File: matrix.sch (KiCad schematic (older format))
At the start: 84 parts

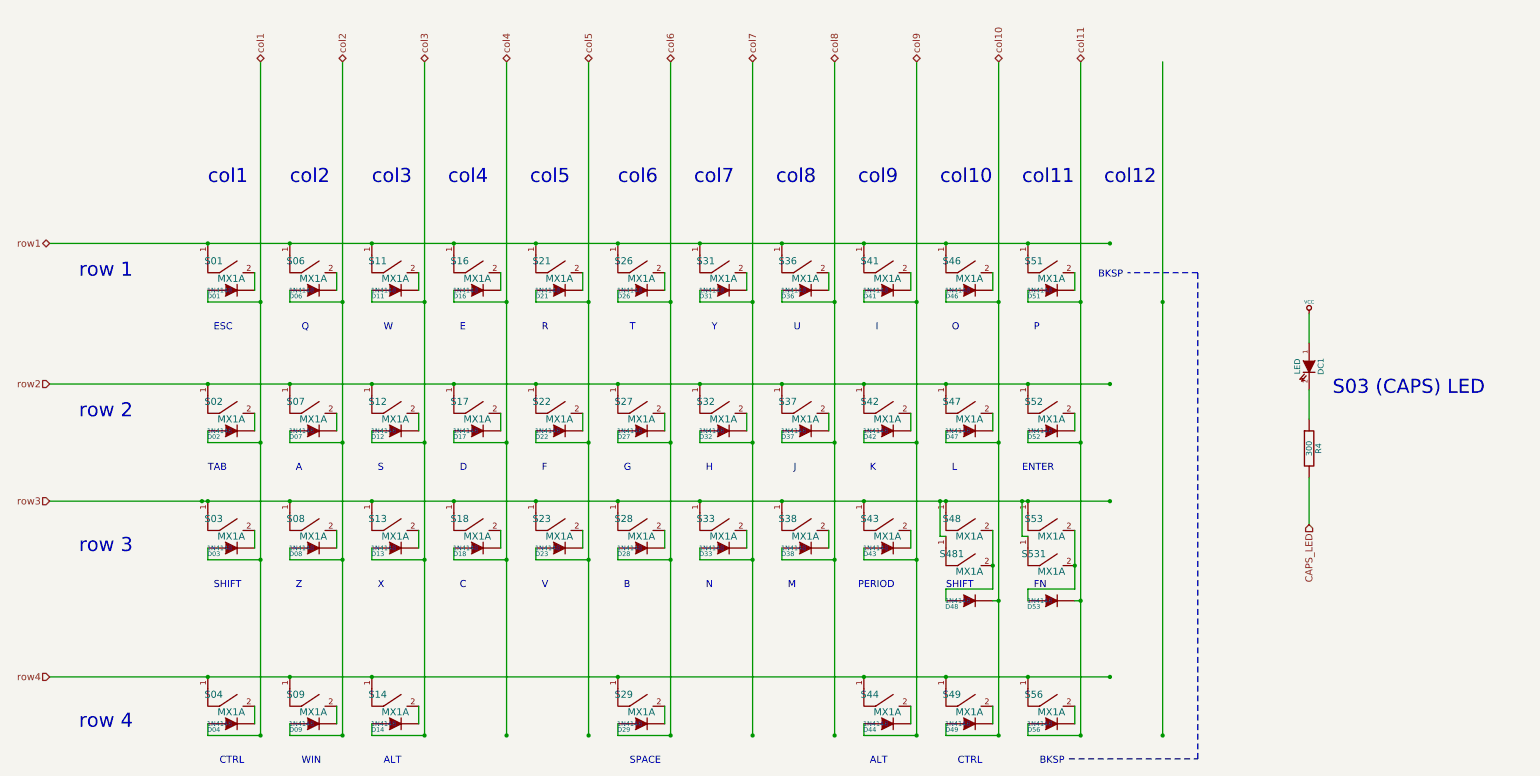
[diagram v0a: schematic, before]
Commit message: Change the cyrstal footprint / correct two wrong diode directions
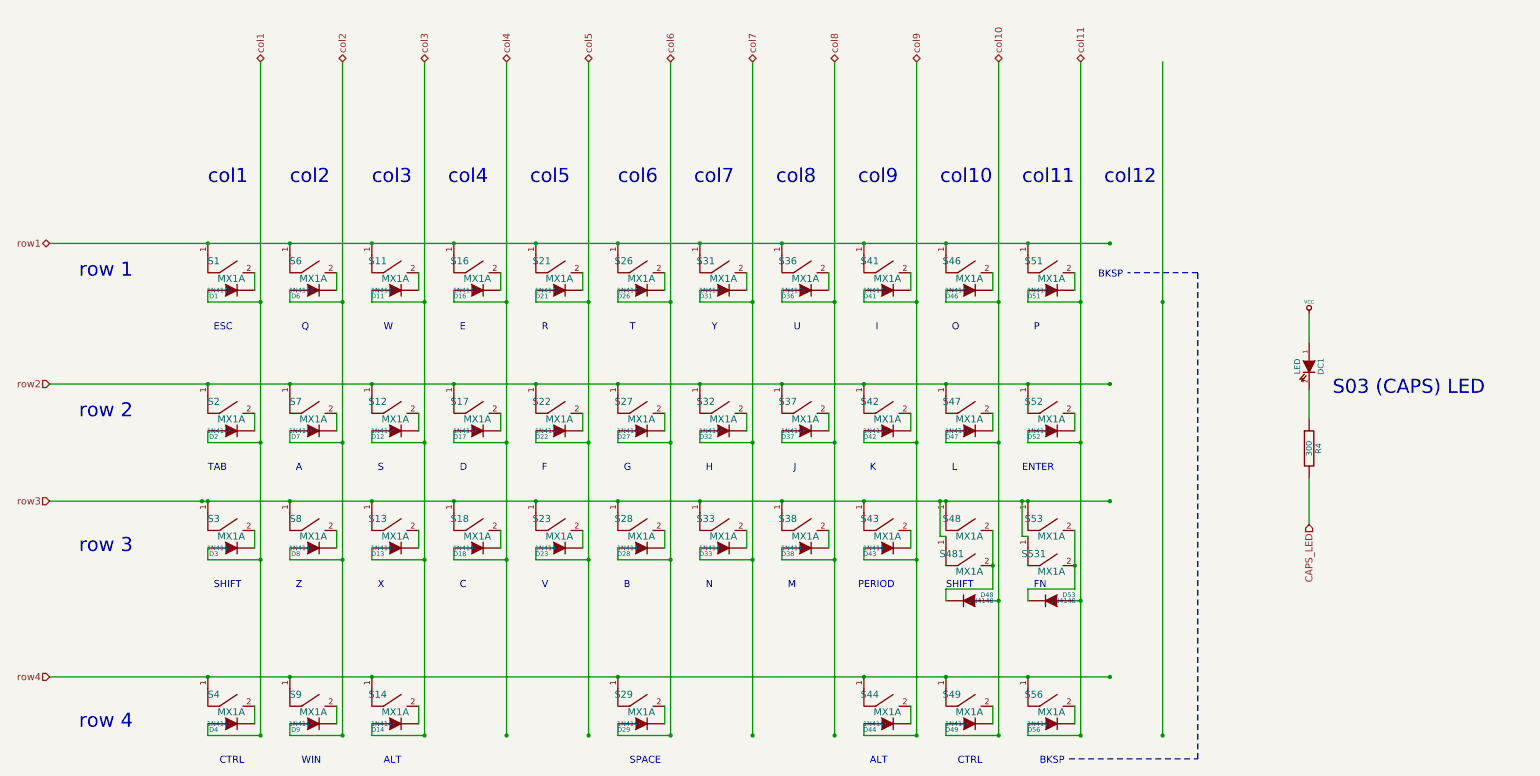
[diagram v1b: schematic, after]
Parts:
- renumbered D01 to D1, D02 to D2, D03 to D3, D04 to D4, D06 to D6, D07 to D7, D08 to D8, D09 to D9, S01 to S1, S02 to S2, S03 to S3, S04 to S4, S06 to S6, S07 to S7, S08 to S8, S09 to S9
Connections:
- net col10: now also D48.1 (A); no longer D48.2 (K)
- net col11: now also D53.1 (A); no longer D53.2 (K)
- net at S48.2, S481.2: now also D48.2 (K); no longer D48.1 (A)
- net at S53.2, S531.2: now also D53.2 (K); no longer D53.1 (A)
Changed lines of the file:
@@
-EESchema Schematic File Version 2  date 11/23/2013 1:19:47 PM
+EESchema Schematic File Version 2
 LIBS:power
 LIBS:mx1a-simple
@@
 LIBS:usb_ports
 LIBS:keyboard-cache
-EELAYER 27 0
+EELAYER 25 0
 EELAYER END
 $Descr A3 16535 11693
@@
 $EndDescr
 $Comp
-L MX1A S01
+L MX1A S1
 U 1 1 5040DD75
 P 3350 3350
-F 0 "S01" H 3200 3600 60  0000 C CNN
+F 0 "S1" H 3200 3600 60  0000 C CNN
 F 1 "MX1A" H 3350 3450 60  0000 C CNN
 F 2 "" H 3350 3350 60  0001 C CNN
@@
 $EndComp
 $Comp
-L MX1A S06
+L MX1A S6
 U 1 1 5040DD84
 P 4050 3350
-F 0 "S06" H 3900 3600 60  0000 C CNN
+F 0 "S6" H 3900 3600 60  0000 C CNN
 F 1 "MX1A" H 4050 3450 60  0000 C CNN
 F 2 "" H 4050 3350 60  0001 C CNN
@@
 $EndComp
 $Comp
-L MX1A S02
+L MX1A S2
 U 1 1 5040DDF7
 P 3350 4550
-F 0 "S02" H 3200 4800 60  0000 C CNN
+F 0 "S2" H 3200 4800 60  0000 C CNN
 F 1 "MX1A" H 3350 4650 60  0000 C CNN
 F 2 "" H 3350 4550 60  0001 C CNN
@@
 $EndComp
 $Comp
-L MX1A S07
+L MX1A S7
 U 1 1 5040DDFD
 P 4050 4550
-F 0 "S07" H 3900 4800 60  0000 C CNN
+F 0 "S7" H 3900 4800 60  0000 C CNN
 F 1 "MX1A" H 4050 4650 60  0000 C CNN
 F 2 "" H 4050 4550 60  0001 C CNN
@@
 $EndComp
 $Comp
-L MX1A S03
+L MX1A S3
 U 1 1 5040DE57
 P 3350 5550
-F 0 "S03" H 3200 5800 60  0000 C CNN
+F 0 "S3" H 3200 5800 60  0000 C CNN
 F 1 "MX1A" H 3350 5650 60  0000 C CNN
 F 2 "" H 3350 5550 60  0001 C CNN
@@
 $EndComp
 $Comp
-L MX1A S08
+L MX1A S8
 U 1 1 5040DE5D
 P 4050 5550
-F 0 "S08" H 3900 5800 60  0000 C CNN
+F 0 "S8" H 3900 5800 60  0000 C CNN
 F 1 "MX1A" H 4050 5650 60  0000 C CNN
 F 2 "" H 4050 5550 60  0001 C CNN
@@
 $EndComp
 $Comp
-L MX1A S09
+L MX1A S9
 U 1 1 5040DEBD
 P 4050 7050
-F 0 "S09" H 3900 7300 60  0000 C CNN
+F 0 "S9" H 3900 7300 60  0000 C CNN
 F 1 "MX1A" H 4050 7150 60  0000 C CNN
 F 2 "" H 4050 7050 60  0001 C CNN
@@
 $EndComp
 $Comp
-L MX1A S04
+L MX1A S4
 U 1 1 5040DEB7
 P 3350 7050
-F 0 "S04" H 3200 7300 60  0000 C CNN
+F 0 "S4" H 3200 7300 60  0000 C CNN
 F 1 "MX1A" H 3350 7150 60  0000 C CNN
 F 2 "" H 3350 7050 60  0001 C CNN
@@
 col11
 $Comp
-L VCC #PWR032
+L VCC #PWR028
 U 1 1 5043970C
 P 12550 3550
-F 0 "#PWR032" H 12550 3650 30  0001 C CNN
+F 0 "#PWR028" H 12550 3650 30  0001 C CNN
 F 1 "VCC" H 12550 3650 30  0000 C CNN
 F 2 "" H 12550 3550 60  0001 C CNN
@@
 $EndComp
 $Comp
-L DIODE D06
+L DIODE D6
 U 1 1 506B1C22
 P 4050 3350
-F 0 "D06" H 3900 3300 40  0000 C CNN
+F 0 "D6" H 3900 3300 40  0000 C CNN
 F 1 "1N4148" H 3950 3350 40  0000 C CNN
 F 2 "" H 4050 3350 60  0001 C CNN
@@
 $EndComp
 $Comp
-L DIODE D02
+L DIODE D2
 U 1 1 506B1C34
 P 3350 4550
-F 0 "D02" H 3200 4500 40  0000 C CNN
+F 0 "D2" H 3200 4500 40  0000 C CNN
 F 1 "1N4148" H 3250 4550 40  0000 C CNN
 F 2 "" H 3350 4550 60  0001 C CNN
@@
 $EndComp
 $Comp
-L DIODE D04
+L DIODE D4
 U 1 1 506B1C3D
 P 3350 7050
-F 0 "D04" H 3200 7000 40  0000 C CNN
+F 0 "D4" H 3200 7000 40  0000 C CNN
 F 1 "1N4148" H 3250 7050 40  0000 C CNN
 F 2 "" H 3350 7050 60  0001 C CNN
@@
 $EndComp
 $Comp
-L DIODE D07
+L DIODE D7
 U 1 1 506B1C46
 P 4050 4550
-F 0 "D07" H 3900 4500 40  0000 C CNN
+F 0 "D7" H 3900 4500 40  0000 C CNN
 F 1 "1N4148" H 3950 4550 40  0000 C CNN
 F 2 "" H 4050 4550 60  0001 C CNN
@@
 $EndComp
 $Comp
-L DIODE D08
+L DIODE D8
 U 1 1 506B1C4F
 P 4050 5550
-F 0 "D08" H 3900 5500 40  0000 C CNN
+F 0 "D8" H 3900 5500 40  0000 C CNN
 F 1 "1N4148" H 3950 5550 40  0000 C CNN
 F 2 "" H 4050 5550 60  0001 C CNN
@@
 $EndComp
 $Comp
-L DIODE D09
+L DIODE D9
 U 1 1 506B428A
 P 4050 7050
-F 0 "D09" H 3900 7000 40  0000 C CNN
+F 0 "D9" H 3900 7000 40  0000 C CNN
 F 1 "1N4148" H 3950 7050 40  0000 C CNN
 F 2 "" H 4050 7050 60  0001 C CNN
@@
 $EndComp
 $Comp
-L DIODE D01
+L DIODE D1
 U 1 1 506B5923
 P 3350 3350
-F 0 "D01" H 3200 3300 40  0000 C CNN
+F 0 "D1" H 3200 3300 40  0000 C CNN
 F 1 "1N4148" H 3250 3350 40  0000 C CNN
 F 2 "" H 3350 3350 60  0001 C CNN
@@
 F 7 "1N4148-0805" H 4700 4800 60  0001 C CNN "Supplier Symbol"
 	1    9650 6000
-	1    0    0    -1
+	-1   0    0    1
 $EndComp
 $Comp
@@
 F 7 "1N4148-0805" H 4850 4800 60  0001 C CNN "Supplier Symbol"
 	1    10350 6000
-	1    0    0    -1
+	-1   0    0    1
 $EndComp
 $Comp
@@
 $EndComp
 $Comp
-L DIODE D03
+L DIODE D3
 U 1 1 506B5DE9
 P 3350 5550
-F 0 "D03" H 3200 5500 40  0000 C CNN
+F 0 "D3" H 3200 5500 40  0000 C CNN
 F 1 "1N4148" H 3250 5550 40  0000 C CNN
 F 2 "" H 3350 5550 60  0001 C CNN

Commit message: Rebuild the project using latest kicad
Rebuild the project using latest kicad, leaving eschematic and pcb
unfinished
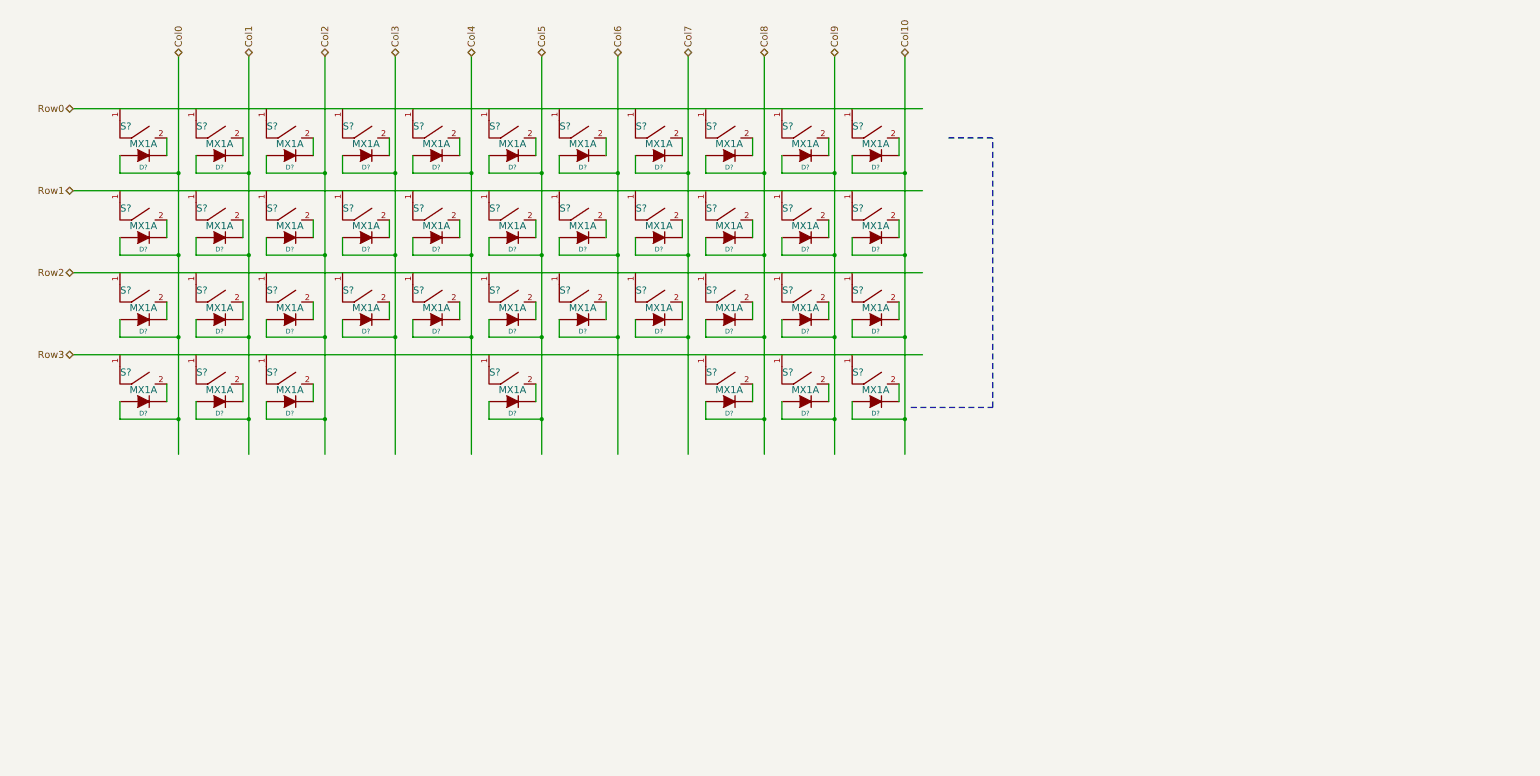
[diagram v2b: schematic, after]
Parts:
- removed D1, D11, D12, D13, D14, D16, D17, D18, D2, D21, D22, D23, D26, D27, D28, D29, D3, D31, D32, D33, D36, D37, D38, D4, D41, D42, D43, D44, D46, D47, D48, D49, D51, D52, D53, D56, D6, D7, D8, D9: 1N4148, symbol DIODE
- removed DC1: LED, symbol LED
- removed R4: 300, symbol R
- removed S1, S11, S12, S13, S14, S16, S17, S18, S2, S21, S22, S23, S26, S27, S28, S29, S3, S31, S32, S33, S36, S37, S38, S4, S41, S42, S43, S44, S46, S47, S48, S481, S49, S51, S52, S53, S531, S56, S6, S7, S8, S9: MX1A, symbol MX1A
- added D? (x40): DIODE, symbol DIODE
- added S? (x40): MX1A, symbol MX1A
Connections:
- net labels added: Col0, Col1, Col10, Col2, Col3, Col4, Col5, Col6, Col7, Col8, Col9, Row0, Row1, Row2, Row3
- net labels removed: CAPS_LED, VCC, col1, col10, col11, col2, col3, col4, col5, col6, col7, col8, col9, row1, row2, row3, row4
- wire segments 145 -> 135
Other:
- note removed: "A"
- note removed: "ALT"
- note removed: "B"
- note removed: "BKSP"
- note removed: "C"
- note removed: "CTRL"
- note removed: "D"
- note removed: "E"
- note removed: "ENTER"
- note removed: "ESC"
- note removed: "F"
- note removed: "FN"
- note removed: "G"
- note removed: "H"
- note removed: "I"
- note removed: "J"
- note removed: "K"
- note removed: "L"
- note removed: "M"
- note removed: "N"
- note removed: "O"
- note removed: "P"
- note removed: "PERIOD"
- note removed: "Q"
- note removed: "R"
- note removed: "S"
- note removed: "S03 (CAPS) LED\n"
- note removed: "SHIFT"
- note removed: "SPACE"
- note removed: "T"
- note removed: "TAB"
- note removed: "U"
- note removed: "V"
- note removed: "W"
- note removed: "WIN"
- note removed: "X"
- note removed: "Y"
- note removed: "Z"
- note removed: "col1"
- note removed: "col10"
- note removed: "col11"
- note removed: "col12"
- note removed: "col2"
- note removed: "col3"
- note removed: "col4"
- note removed: "col5"
- note removed: "col6"
- note removed: "col7"
- note removed: "col8"
- note removed: "col9"
- note removed: "row 1"
- note removed: "row 2"
- note removed: "row 3"
- note removed: "row 4"

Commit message: Minor Changes
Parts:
- D1, D10, D11, D12, D13, D14, D15, D16, D17, D18, D19, D2, D20, D21, D22, D23, D24, D25, D26, D27, D28, D29, D3, D30, D31, D32, D33, D34, D35, D36, D37, D38, D39, D4, D40, D5, D6, D7, D8, D9: renamed from D?; footprint (none) -> SM0805:SM0805D
- S1, S10, S11, S12, S13, S14, S15, S16, S17, S18, S19, S2, S20, S21, S22, S23, S24, S25, S26, S27, S28, S29, S3, S30, S31, S32, S33, S34, S35, S36, S37, S38, S39, S4, S40, S5, S6, S7, S8, S9: renamed from S?; footprint (none) -> MX1A_alps:MX1ALPS
